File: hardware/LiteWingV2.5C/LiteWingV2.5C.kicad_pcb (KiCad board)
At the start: 2 copper layers, 100 x 100 mm, 95 parts, among them IC1 TP4056, J1 USB_C_Receptacle_USB2.0, J10 Conn_01x02_Female, J11 Conn_01x09, J12 Conn_01x06, J13 Conn_01x07, J14 Conn_01x02, J2 JST XH 2P 2.50mm SMD Hoz, J3 Conn_01x06, J4 Conn_01x06, J5 Conn_01x06, J6 Conn_01x06, J7 Conn_01x02_Female, J8 Conn_01x02_Female, J9 Conn_01x02_Female, SW1 MST22D18G2_125, SW2 Tactile Switch 3x4x2, SW3 Tactile Switch 3x4x2, T1 IRLML6344TRPBF, T2 IRLML6344TRPBF, T3 IRLML6344TRPBF, T4 IRLML6344TRPBF, U1 AO3401A, U2 SPX3819M5-L-3-3/TR, U5 CH340K, U6 2N27002DW, U7 MPU-6050, U8 ESP32-S3-WROOM-1

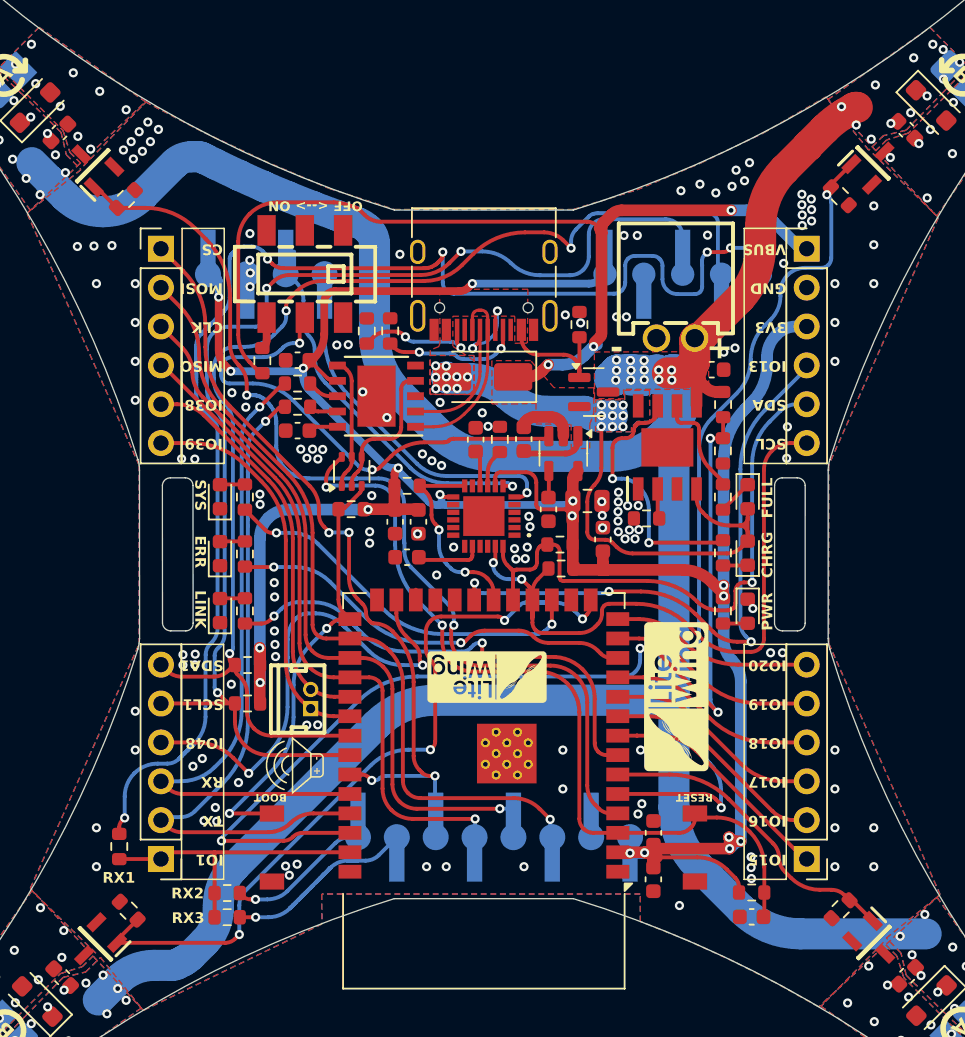
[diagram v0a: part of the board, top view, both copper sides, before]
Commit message: Update to remove USB to serial converter and use native USB on ESP32-S3 instead.
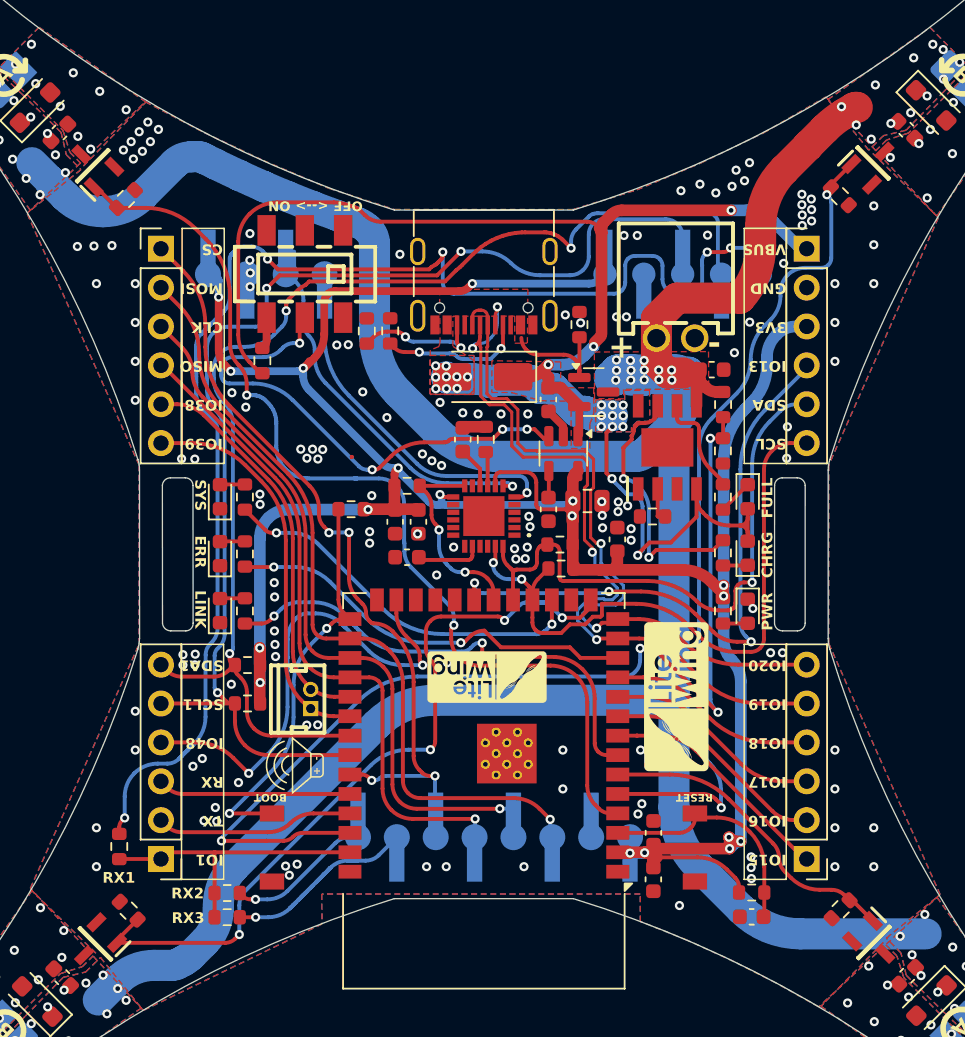
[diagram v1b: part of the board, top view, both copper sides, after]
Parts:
- removed C6, C7: 100nF, Capacitor_SMD:C_0603_1608Metric
- removed R10, R9: 1K, Resistor_SMD:R_0603_1608Metric
- removed U5: CH340K, ch340k:ESSOP-10_3.9x4.9mm_P1.00mm
- removed U6: 2N27002DW, Package_TO_SOT_SMD:SOT-363_SC-70-6
- J1: value USB_C_Receptacle_USB2.0 -> USB_C_Receptacle_USB2.0_16P; footprint Connector_USB:USB_C_Receptacle_HRO_TYPE-C-31-M-12 -> SL_Power:USB_C_Receptacle_G-Switch_GT-USB-7010ASV
- moved C1 3.05 mm to (151.6, 84.1), turned to -90 degrees
- moved C4 0.94 mm to (156.1, 93.2)
- moved R15 0.92 mm to (147.5, 86.7)
- moved C8 0.84 mm to (146.0, 86.7)
- moved R5 0.41 mm to (158.4, 91.7)
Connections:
- J1 pad A6: /D+ -> /USB D+
- J1 pad A7: /D- -> /USB D-
- J1 pad B6: /D+ -> /USB D+
- J1 pad B7: /D- -> /USB D-
- J2 pad 1: +BATT -> GND
- J2 pad 2: GND -> +BATT
- J3 pad 5: /IO19 -> /USB D-
- J3 pad 6: /IO20 -> /USB D+
- U8 pad 13: /IO19 -> /USB D-
- U8 pad 14: /IO20 -> /USB D+
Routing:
- net /USB D-: track 0.00 -> 50.3 mm, vias 0 -> 4
- net /USB D+: track 0.00 -> 46.6 mm, vias 0 -> 2
- net /EN: track 54.6 -> 14.7 mm, vias 2 -> 0
- net /TX: track 44.0 -> 12.4 mm, vias 1 -> 0
- net /RX: track 43.1 -> 12.0 mm, vias 1 -> 0
- net /D-: track 13.7 -> 0.00 mm, vias 2 -> 0
- net /IO19: track 13.7 -> 0.00 mm
- net /IO20: track 13.2 -> 0.00 mm
- net /D+: track 12.5 -> 0.00 mm
- net /DTR: track 9.65 -> 0.00 mm
- net /RTS: track 8.79 -> 0.00 mm
- net +3V3: track 184.0 -> 180.0 mm
- net +BATT: track 195.1 -> 198.6 mm
- net /IO0: track 28.0 -> 25.1 mm
- net Net-(U5-TXD): track 2.07 -> 0.00 mm
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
